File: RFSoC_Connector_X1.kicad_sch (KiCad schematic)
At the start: 1 part, among them J201 ${FAMILY}

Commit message: Routing the Digital Part
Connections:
- net B84.L1N / D01 AW5 renamed B84.L1N_D01_AW5
- net B84.L1P / D00 AW6  renamed B84.L1P_D00_AW6
- net B84.L2N / D03 AW3 renamed B84.L2N_D03_AW3
- net B84.L2P / D02 AW4 renamed B84.L2P_D02_AW4
- net B84.L3N / D05 AV2 renamed B84.L3N_D05_AV2
- net B84.L3P / D04 AV3  renamed B84.L3P_D04_AV3
- net B84.L4P / D06 AU2 renamed B84.L4P_D06_AU2
- net B84.L5N / D09 AV5 renamed B84.L5N_D09_AV5
- net B84.L5P / D08 AV6  renamed B84.L5P_D08_AV6
- net B84.L6N / D11 AU3 renamed B84.L6N_D11_AU3
- net B84.L6P / D10 AU4 renamed B84.L6P_D10_AU4
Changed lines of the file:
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@@
 	(wire
 		(pts
-			(xy 130.81 182.88) (xy 170.18 182.88)
+			(xy 130.81 182.88) (xy 171.45 182.88)
 		)
 		(stroke
@@
 	(wire
 		(pts
-			(xy 29.21 177.8) (xy 72.39 177.8)
+			(xy 29.21 177.8) (xy 83.82 177.8)
 		)
 		(stroke
@@
 	(wire
 		(pts
-			(xy 207.01 187.96) (xy 248.92 187.96)
+			(xy 207.01 187.96) (xy 251.46 187.96)
 		)
 		(stroke
@@
 	(wire
 		(pts
-			(xy 130.81 185.42) (xy 170.18 185.42)
+			(xy 130.81 185.42) (xy 171.45 185.42)
 		)
 		(stroke
@@
 	(wire
 		(pts
-			(xy 29.21 182.88) (xy 72.39 182.88)
+			(xy 29.21 182.88) (xy 83.82 182.88)
 		)
 		(stroke
@@
 	(wire
 		(pts
-			(xy 303.53 187.96) (xy 347.98 187.96)
+			(xy 303.53 187.96) (xy 350.52 187.96)
 		)
 		(stroke
@@
 	(wire
 		(pts
-			(xy 29.21 187.96) (xy 72.39 187.96)
+			(xy 29.21 187.96) (xy 83.82 187.96)
 		)
 		(stroke
@@
 	(wire
 		(pts
-			(xy 29.21 180.34) (xy 72.39 180.34)
+			(xy 29.21 180.34) (xy 83.82 180.34)
 		)
 		(stroke
@@
 	(wire
 		(pts
-			(xy 130.81 187.96) (xy 170.18 187.96)
+			(xy 130.81 187.96) (xy 171.45 187.96)
 		)
 		(stroke
@@
 	(wire
 		(pts
-			(xy 130.81 177.8) (xy 170.18 177.8)
+			(xy 130.81 177.8) (xy 171.45 177.8)
 		)
 		(stroke
@@
 	(wire
 		(pts
-			(xy 29.21 185.42) (xy 72.39 185.42)
+			(xy 29.21 185.42) (xy 83.82 185.42)
 		)
 		(stroke
@@
 		)
 	)
+	(hierarchical_label "B84.L5N_D09_AV5"
+		(shape input)
+		(at 171.45 177.8 0)
+		(effects
+			(font
+				(size 1.27 1.27)
+			)
+			(justify left)
+		)
+	)
+	(hierarchical_label "B84.L1N_D01_AW5"
+		(shape input)
+		(at 171.45 187.96 0)
+		(effects
+			(font
+				(size 1.27 1.27)
+			)
+			(justify left)
+		)
+	)
 	(hierarchical_label "ADC225_VIN23_N "
 		(shape input)
@@
 		)
 	)
+	(hierarchical_label "B84.L1P_D00_AW6"
+		(shape input)
+		(at 83.82 187.96 0)
+		(effects
+			(font
+				(size 1.27 1.27)
+			)
+			(justify left)
+		)
+	)
 	(hierarchical_label "ADC225_VIN01_P "
 		(shape input)
@@
 		)
 	)
+	(hierarchical_label "B84.L5P_D08_AV6"
+		(shape input)
+		(at 83.82 177.8 0)
+		(effects
+			(font
+				(size 1.27 1.27)
+			)
+			(justify left)
+		)
+	)
 	(hierarchical_label "ADC224_VIN01_N "
 		(shape input)
@@
 		)
 	)
+	(hierarchical_label "B84.L2P_D02_AW4"
+		(shape input)
+		(at 83.82 185.42 0)
+		(effects
+			(font
+				(size 1.27 1.27)
+			)
+			(justify left)
+		)
+	)
 	(hierarchical_label "ADC226_VIN23_N"
 		(shape input)
@@
 		)
 	)
+	(hierarchical_label "B84.L6N_D11_AU3"
+		(shape input)
+		(at 350.52 187.96 0)
+		(effects
+			(font
+				(size 1.27 1.27)
+			)
+			(justify left)
+		)
+	)
 	(hierarchical_label "ADC225_VIN23_P "
 		(shape input)
@@
 		)
 	)
+	(hierarchical_label "B84.L2N_D03_AW3"
+		(shape input)
+		(at 171.45 185.42 0)
+		(effects
+			(font
+				(size 1.27 1.27)
+			)
+			(justify left)
+		)
+	)
 	(hierarchical_label "ADC227_VIN23_N"
 		(shape input)
@@
 		)
 	)
+	(hierarchical_label "B84.L3P_D04_AV3"
+		(shape input)
+		(at 83.82 182.88 0)
+		(effects
+			(font
+				(size 1.27 1.27)
+			)
+			(justify left)
+		)
+	)
+	(hierarchical_label "B84.L3N_D05_AV2"
+		(shape input)
+		(at 171.45 182.88 0)
+		(effects
+			(font
+				(size 1.27 1.27)
+			)
+			(justify left)
+		)
+	)
 	(hierarchical_label "ADC226_VIN01_N"
 		(shape input)
@@
 		)
 	)
+	(hierarchical_label "B84.L4P_D06_AU2"
+		(shape input)
+		(at 83.82 180.34 0)
+		(effects
+			(font
+				(size 1.27 1.27)
+			)
+			(justify left)
+		)
+	)
 	(hierarchical_label "ADC224_VIN01_P "
 		(shape input)
@@
 		(effects
 			(font
+				(size 1.27 1.27)
+			)
+			(justify left)
+		)
+	)
+	(hierarchical_label "B84.L6P_D10_AU4"
+		(shape input)
+		(at 251.46 187.96 0)
+		(effects
+			(font

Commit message: Routing almost complete
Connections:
- net DAC228_VOUT0_N  renamed DAC228_VOUT0_N
- net DAC228_VOUT0_P  renamed DAC228_VOUT0_P
- net DAC229_VOUT3_P  renamed DAC229_VOUT3_P
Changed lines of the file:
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@@
-		)
-	)
-	(label "DAC228_VOUT0_N "
-		(at 53.34 96.52 0)
-		(effects
-			(font
-				(size 1.27 1.27)
-			)
-			(justify left bottom)
 		)
 	)
@@
 		)
 	)
-	(label "DAC229_VOUT3_N"
-		(at 53.34 43.18 0)
-		(effects
-			(font
-				(size 1.27 1.27)
-			)
-			(justify left bottom)
-		)
-	)
 	(label "B84.L5N {slash} D09 AV5"
 		(at 151.13 177.8 0)
@@
 		)
 	)
-	(label "DAC229_VOUT3_P "
-		(at 53.34 45.72 0)
-		(effects
-			(font
-				(size 1.27 1.27)
-			)
-			(justify left bottom)
-		)
-	)
 	(label "DAC229_VOUT2_P"
 		(at 53.34 53.34 0)
@@
 		)
 	)
-	(label "DAC228_VOUT0_P "
-		(at 53.34 99.06 0)
-		(effects
-			(font
-				(size 1.27 1.27)
-			)
-			(justify left bottom)
-		)
-	)
 	(label "VCM226_01"
 		(at 327.66 149.86 0)
@@
 		)
 	)
+	(hierarchical_label "DAC228_VOUT0_N"
+		(shape input)
+		(at 69.85 96.52 0)
+		(effects
+			(font
+				(size 1.27 1.27)
+			)
+			(justify left)
+		)
+	)
 	(hierarchical_label "ADC224_VIN23_N "
 		(shape input)
@@
 		)
 	)
+	(hierarchical_label "DAC229_VOUT3_P"
+		(shape input)
+		(at 69.85 45.72 0)
+		(effects
+			(font
+				(size 1.27 1.27)
+			)
+			(justify left)
+		)
+	)
 	(hierarchical_label "B84.L5N_D09_AV5"
 		(shape input)
@@
 		)
 	)
+	(hierarchical_label "DAC228_VOUT0_P"
+		(shape input)
+		(at 69.85 99.06 0)
+		(effects
+			(font
+				(size 1.27 1.27)
+			)
+			(justify left)
+		)
+	)
 	(hierarchical_label "ADC226_VIN01_N"
 		(shape input)
@@
 		(effects
 			(font
+				(size 1.27 1.27)
+			)
+			(justify left)
+		)
+	)
+	(hierarchical_label "DAC229_VOUT3_N"
+		(shape input)
+		(at 69.85 43.18 0)
+		(effects
+			(font

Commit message: Routing almost complete
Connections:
- net DAC228_VOUT1_N  renamed DAC228_VOUT1_N
- net DAC228_VOUT1_P  renamed DAC228_VOUT1_P
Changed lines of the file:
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@@
-		)
-	)
-	(label "DAC228_VOUT1_P "
-		(at 53.34 91.44 0)
-		(effects
-			(font
-				(size 1.27 1.27)
-			)
-			(justify left bottom)
 		)
 	)
@@
 		)
 	)
-	(label "DAC229_VOUT2_N"
-		(at 53.34 50.8 0)
-		(effects
-			(font
-				(size 1.27 1.27)
-			)
-			(justify left bottom)
+	(label "DAC229_VOUT3_P"
+		(at 69.85 45.72 180)
+		(effects
+			(font
+				(size 1.27 1.27)
+			)
+			(justify right bottom)
 		)
 	)
@@
 		)
 	)
+	(label "DAC229_VOUT2_P"
+		(at 69.85 53.34 180)
+		(effects
+			(font
+				(size 1.27 1.27)
+			)
+			(justify right bottom)
+		)
+	)
 	(label "+1V2_BIAS_OUT"
 		(at 228.6 45.72 0)
@@
 		)
 	)
+	(label "DAC229_VOUT3_N"
+		(at 69.85 43.18 180)
+		(effects
+			(font
+				(size 1.27 1.27)
+			)
+			(justify right bottom)
+		)
+	)
 	(label "DAC229_VOUT1_P"
 		(at 53.34 60.96 0)
@@
 		)
 	)
+	(label "DAC229_VOUT2_N"
+		(at 69.85 50.8 180)
+		(effects
+			(font
+				(size 1.27 1.27)
+			)
+			(justify right bottom)
+		)
+	)
 	(label "B84.L8N {slash} D15 AT6"
 		(at 327.66 182.88 0)
@@
 		)
 	)
-	(label "DAC229_VOUT2_P"
-		(at 53.34 53.34 0)
-		(effects
-			(font
-				(size 1.27 1.27)
-			)
-			(justify left bottom)
-		)
-	)
-	(label "DAC228_VOUT1_N "
-		(at 53.34 88.9 0)
-		(effects
-			(font
-				(size 1.27 1.27)
-			)
-			(justify left bottom)
-		)
-	)
 	(label "+ADC_AVCC_AUX_1V8"
 		(at 228.6 167.64 0)
@@
 		)
 	)
+	(hierarchical_label "DAC228_VOUT1_N"
+		(shape output)
+		(at 69.85 88.9 0)
+		(effects
+			(font
+				(size 1.27 1.27)
+			)
+			(justify left)
+		)
+	)
 	(hierarchical_label "DAC228_VOUT0_N"
-		(shape input)
+		(shape output)
 		(at 69.85 96.52 0)
 		(effects
@@
 		)
 	)
-	(hierarchical_label "DAC229_VOUT3_P"
-		(shape input)
-		(at 69.85 45.72 0)
-		(effects
-			(font
-				(size 1.27 1.27)
-			)
-			(justify left)
-		)
-	)
 	(hierarchical_label "B84.L5N_D09_AV5"
 		(shape input)
@@
 		)
 	)
+	(hierarchical_label "DAC228_VOUT1_P"
+		(shape output)
+		(at 69.85 91.44 0)
+		(effects
+			(font
+				(size 1.27 1.27)
+			)
+			(justify left)
+		)
+	)
 	(hierarchical_label "B84.L6N_D11_AU3"
 		(shape input)
@@
 	)
 	(hierarchical_label "DAC228_VOUT0_P"
-		(shape input)
+		(shape output)
 		(at 69.85 99.06 0)
 		(effects
@@
 		(effects
 			(font
-				(size 1.27 1.27)
-			)
-			(justify left)
-		)
-	)
-	(hierarchical_label "DAC229_VOUT3_N"
-		(shape input)
-		(at 69.85 43.18 0)
-		(effects
-			(font

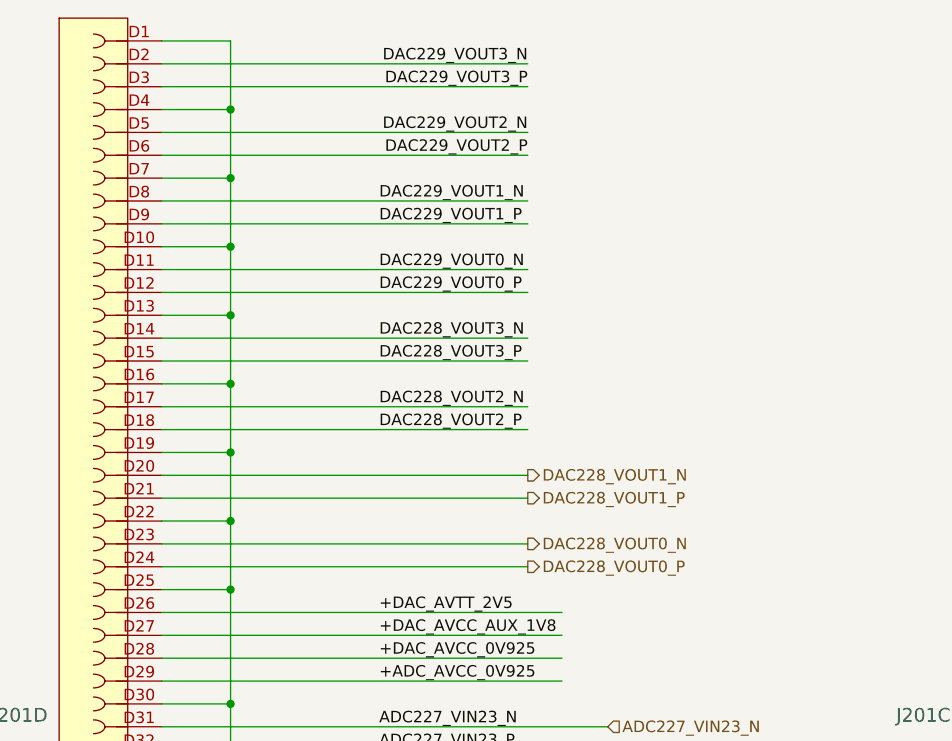
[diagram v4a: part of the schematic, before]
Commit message: GND Vias added
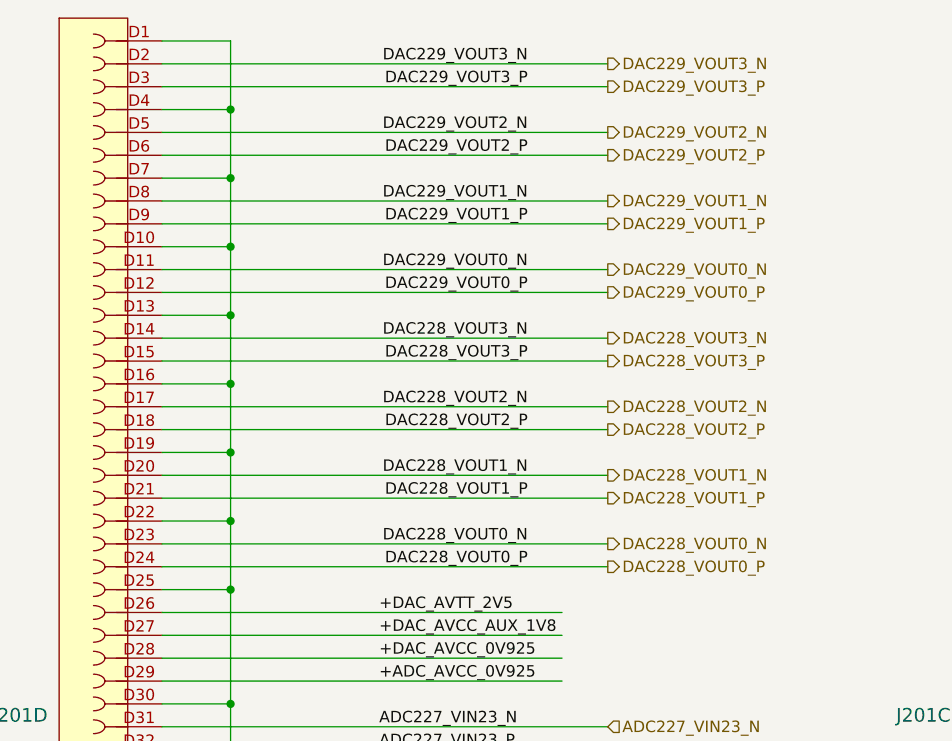
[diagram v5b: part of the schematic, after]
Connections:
- net ADC224_VIN01_N  renamed ADC224_VIN01_N
- net ADC224_VIN01_P  renamed ADC224_VIN01_P
- net ADC224_VIN23_N  renamed ADC224_VIN23_N
- net ADC224_VIN23_P  renamed ADC224_VIN23_P
- net ADC225_VIN01_P  renamed ADC225_VIN01_P
- net ADC225_VIN23_N  renamed ADC225_VIN23_N
- net ADC225_VIN23_P  renamed ADC225_VIN23_P
- net ADC226_VIN01_P  renamed ADC226_VIN01_P
- net ADC227_VIN01_N  renamed ADC227_VIN01_N
- net ADC227_VIN01_P  renamed ADC227_VIN01_P
- net ADC227_VIN23_P  renamed ADC227_VIN23_P
- net DAC228_VOUT2_N  renamed DAC228_VOUT2_N
- net DAC228_VOUT2_P  renamed DAC228_VOUT2_P
- net DAC228_VOUT3_P  renamed DAC228_VOUT3_P
- net DAC229_VOUT0_N  renamed DAC229_VOUT0_N
- net DAC229_VOUT0_P  renamed DAC229_VOUT0_P

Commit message: WIP snapshot
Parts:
- renumbered J201 to J5001
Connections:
- net +1V2_BIAS_OUT renamed +1V2_CLK_BIAS
- net +3V3_EXTERNAL  renamed +3V3D
- net B84.L10N / D19 AV7 renamed B84.L10N_D19_AV7
- net B84.L10P / D18 AU7  renamed B84.L10P_D18_AU7
- net B84.L11N / D21 AR6 renamed B84.L11N_D21_AR6
- net B84.L11P / D20 AR7 renamed B84.L11P_D20_AR7
- net B84.L12N / D23 AP5 renamed B84.L12N_D23_AP5
- net B84.L12P / D22 AP6 renamed B84.L12P_D22_AP6
- net B84.L7N / D13 AU5 renamed B84.L7N_D13_AU5
- net B84.L7P / D12 AT5 renamed B84.L7P_D12_AT5
- net B84.L8N / D15 AT6 renamed B84.L8N_D15_AT6
- net B84.L8P / D14 AT7 renamed B84.L8P_D14_AT7
- net B84.L9N / D17 AV8 renamed B84.L9N_D17_AV8
- net B84.L9P / D16 AU8 renamed B84.L9P_D16_AU8
- net SYSCLOCK_1V2_N B69.L11N H16 renamed SYSCLOCK_62M5_1V2_N
- net SYSCLOCK_1V2_P B69.L11P H17 renamed SYSCLOCK_62M5_1V2_P
- net SYSREF_1V2_N B69.L12N J18 renamed SYSREF_7M_1V2_N
- net SYSREF_1V2_P B69.L12P J19 renamed SYSREF_7M_1V2_P
- net SYSREF_N renamed SYSREF_7M_N
- net SYSREF_P renamed SYSREF_7M_P
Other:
- note added: "Fixme: Vdd for I/O banks seems to be missing"
- moved on the sheet: J5001A, J5001B, J5001C, J5001D

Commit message: Update project files and backups
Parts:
- added C5001, C5002: 1uF, Capacitors SMD:CAPC1005X55N, symbol CERN_Linux:Capacitors SMD/CC0402_1UF_10V_10%_X5R
- added R5001: 0, Resistors SMD:RESC1005X40N, symbol CERN:Resistors SMD/R0402_0R_JUMPER
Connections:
- net B84.L4N / D07 AU1  is gone; now on net B84.L4N_D07_AU1: J5001.C56
- net +VCCO_84: now also C5002.1, R5001.2
- net GND: now also C5001.2, C5002.2
- net +3V3D renamed +3V3_EXTERNAL 
- net +3V3_EXTERNAL : now also C5001.1, R5001.1
- net +ADC_AVCC_0V925 renamed +ADC_AVCC_0V925_NC1
- net +ADC_AVCC_0V925_NC1: no longer J5001.C29
- net +ADC_AVCC_AUX_1V8 renamed +ADC_AVCC_AUX_1V8_NC1
- net +ADC_AVCC_AUX_1V8_NC1: no longer J5001.A51
- net +DAC_AVCC_0V925 renamed +DAC_AVCC_0V925_NC2
- net +DAC_AVCC_0V925  renamed +DAC_AVCC_0V925_NC1
- net +DAC_AVCC_AUX_1V8 renamed +DAC_AVCC_AUX_1V8_NC2
- net +DAC_AVCC_AUX_1V8_NC2: no longer J5001.D27
- net +DAC_AVTT_2V5  renamed +DAC_AVTT_2V5_NC1
- net +DAC_AVTT_2V5_NC1: no longer J5001.C26
- new net +ADC_AVCC_0V925_NC2: J5001.C29
- new net +ADC_AVCC_AUX_1V8_NC2: J5001.A51
- new net +DAC_AVCC_AUX_NC1: J5001.D27
- new net +DAC_AVTT_2V5_NC2: J5001.C26
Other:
- note added: "SYSCLOCK_1V2_P B69.L11P H17 SYSCLOCK_1V2_N B69.L11N H16"
- note added: "SYSREF_1V2_P B69.L12P J19 SYSREF_1V2_N B69.L12N J18"
- note added: "The +1V8_EXTERNAL and +3V3_EXTERNAL are supply outputs that are to be used to power bank I/O rails and light load peripherals"
